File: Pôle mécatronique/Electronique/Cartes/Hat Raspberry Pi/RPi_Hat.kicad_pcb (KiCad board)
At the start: 2 copper layers, 65 x 59 mm, 29 parts, among them J1 Conn_02x03_Odd_Even, J2 RPi_GPIO, J3 Conn_01x02, U1 XBee, U2 MCP25625-x-SS, Y1 8MHz

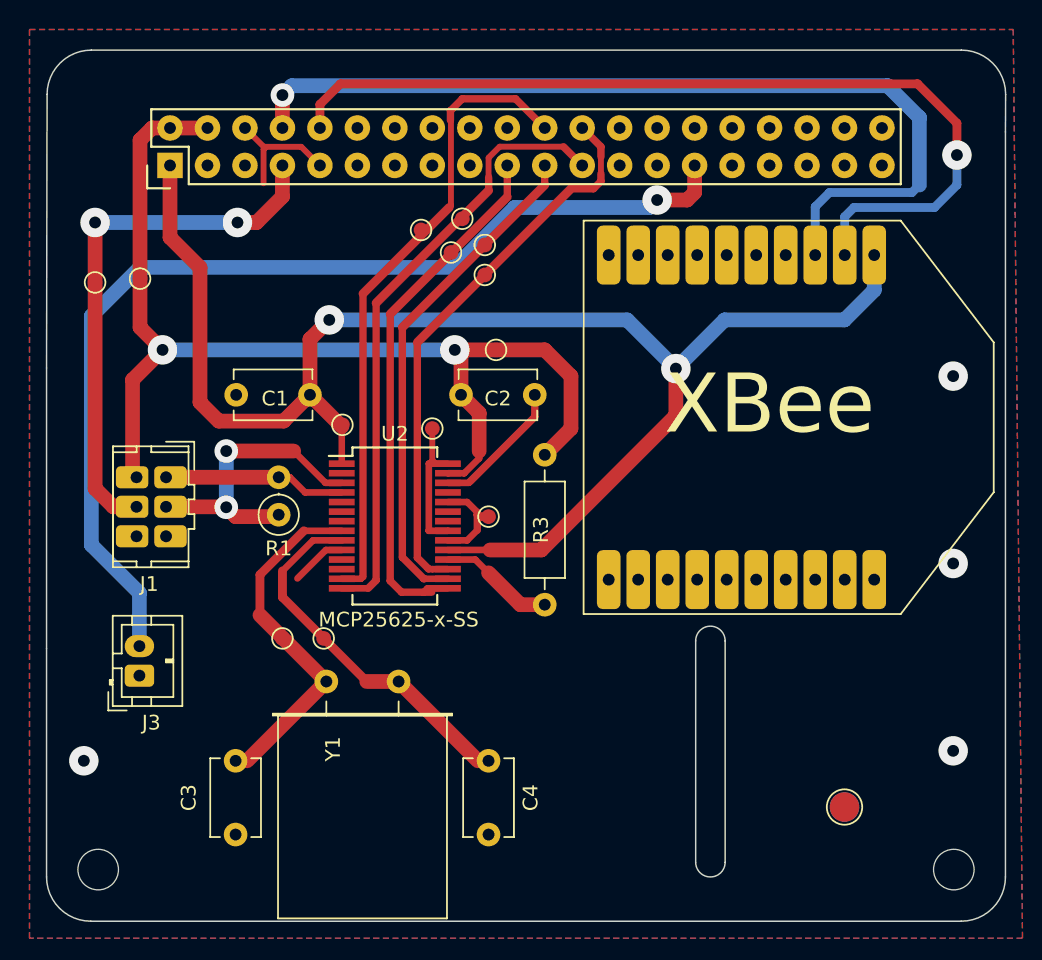
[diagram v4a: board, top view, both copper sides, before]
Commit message: Udpate HAT
Sérigraphie
Points de tests
Arret d'urgence
I2C
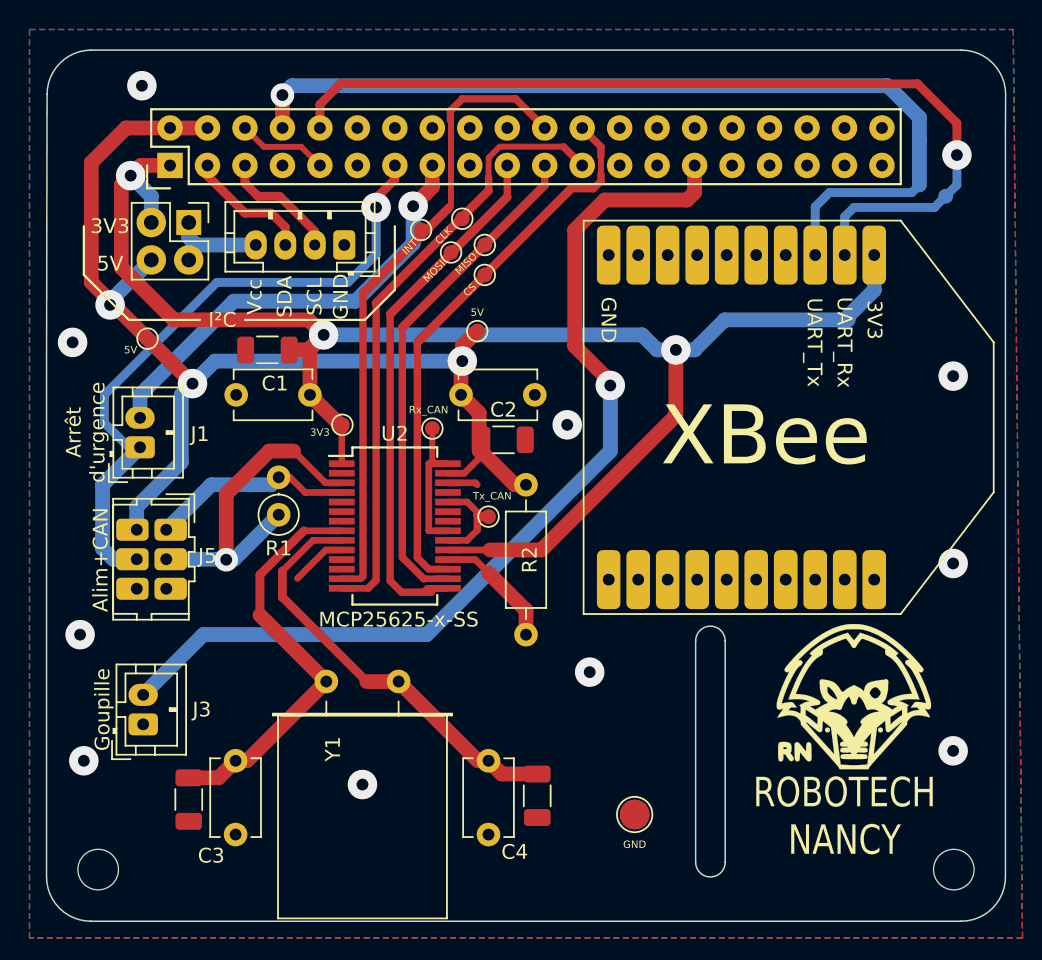
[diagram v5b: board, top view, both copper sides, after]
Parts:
- removed  : TestPoint_Pad_D1.0mm, TestPoint:TestPoint_Pad_D1.0mm (x2)
- removed the ? at (114.3, 86.4)
- removed R3: 5k, Resistor_THT:R_Axial_DIN0207_L6.3mm_D2.5mm_P10.16mm_Horizontal
- removed the REF** at (66.5, 50.5)
- removed the REF** at (114.3, 86.4)
- removed the REF** at (86.4, 60.7)
- removed the REF** at (87.6, 48.8)
- removed the REF** at (89.9, 48.3)
- removed the REF** at (90.7, 55.4)
- removed the REF** at (90.2, 66.7)
- removed the REF** at (88.4, 46.5)
- removed the REF** at (80.3, 60.5)
- removed the REF** at (89.9, 50.3)
- removed the REF** at (63.5, 50.8)
- added G***: LOGO, Logos:logoRobotechNancy10x10, F.Cu at (114.9, 78.7)
- added G***: LOGO, Logos:logoRobotechNancy10x10, B.Cu at (114.9, 78.7)
- added J1: Arrêt d'urgence, Connector_JST:JST_PH_B2B-PH-K_1x02_P2.00mm_Vertical, F.Cu at (66.5, 62.0)
- added J2: RPi_GPIO, Connector_JST:JST_PH_B4B-PH-K_1x04_P2.00mm_Vertical, F.Cu at (80.4, 48.3)
- added J4: Tension I2C, Connector_PinHeader_2.54mm:PinHeader_2x02_P2.54mm_Vertical, F.Cu at (69.8, 46.7)
- added R2: 5k, Resistor_THT:R_Axial_DIN0207_L6.3mm_D2.5mm_P10.16mm_Horizontal, F.Cu at (92.7, 64.5)
- added REF**: C_1206_3216Metric, Capacitor_SMD:C_1206_3216Metric, F.Cu at (93.5, 85.6)
- added REF**: C_1206_3216Metric, Capacitor_SMD:C_1206_3216Metric, F.Cu at (75.2, 55.4)
- added REF**: C_1206_3216Metric, Capacitor_SMD:C_1206_3216Metric, F.Cu at (69.8, 85.9)
- added REF**: C_1206_3216Metric, Capacitor_SMD:C_1206_3216Metric, F.Cu at (91.2, 61.5)
- added TP1: TestPoint, TestPoint:TestPoint_Pad_D1.0mm, B.Cu at (64.8, 63.8)
- added TP10: TestPoint, TestPoint:TestPoint_Pad_D1.0mm, F.Cu at (89.9, 50.3)
- added TP11: TestPoint, TestPoint:TestPoint_Pad_D1.0mm, B.Cu at (114.6, 53.3)
- added TP12: TestPoint, TestPoint:TestPoint_Pad_D1.0mm, F.Cu at (89.4, 54.1)
- added TP13: TestPoint, TestPoint:TestPoint_Pad_D1.0mm, F.Cu at (90.2, 66.7)
- added TP14: TestPoint, TestPoint:TestPoint_Pad_D1.0mm, F.Cu at (86.4, 60.7)
- added TP15: TestPoint, TestPoint:TestPoint_Pad_D2.0mm, F.Cu at (100.1, 86.9)
- added TP16: TestPoint, TestPoint:TestPoint_Pad_D2.0mm, B.Cu at (100.1, 86.9)
- added TP2: TestPoint, TestPoint:TestPoint_Pad_D1.0mm, B.Cu at (67.1, 57.9)
- added TP3: TestPoint, TestPoint:TestPoint_Pad_D1.0mm, B.Cu at (121.2, 45.0)
- added TP4: TestPoint, TestPoint:TestPoint_Pad_D1.0mm, B.Cu at (119.4, 41.1)
- added TP5: TestPoint, TestPoint:TestPoint_Pad_D1.0mm, F.Cu at (80.3, 60.5)
- added TP6: TestPoint, TestPoint:TestPoint_Pad_D1.0mm, F.Cu at (67.1, 54.6)
- added TP7: TestPoint, TestPoint:TestPoint_Pad_D1.0mm, F.Cu at (88.4, 46.5)
- added TP8: TestPoint, TestPoint:TestPoint_Pad_D1.0mm, F.Cu at (87.6, 48.8)
- added TP9: TestPoint, TestPoint:TestPoint_Pad_D1.0mm, F.Cu at (89.9, 48.3)
- J3: value Conn_01x02 -> Goupille
- J5: renamed from J1; value Conn_02x03_Odd_Even -> I2C
- J6: renamed from J2; value RPi_GPIO -> Vcc I2C
- moved J5 3.56 mm to (68.3, 67.6)
- moved J3 3.31 mm to (66.8, 80.8)
- renumbered REF** to Test_INT
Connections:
- J6 pad 13: unconnected-(J2-Pad13) -> cmd_relais
- J6 pad 15: unconnected-(J2-Pad15) -> /RPi_GPIO/cmd_relais_RPI
- J6 pad 3: unconnected-(J2-Pad3) -> SDA
- J6 pad 5: unconnected-(J2-Pad5) -> SCL
- J6 pad 7: cmd_relais -> unconnected-(J6-Pad7)
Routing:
- net /RPi_GPIO/cmd_relais_RPI: track 0.00 -> 30.1 mm, vias 0 -> 1
- net GND: track 24.5 -> 13.7 mm, vias 4 -> 10
- net SDA: track 0.00 -> 8.61 mm
- net SCL: track 0.00 -> 8.21 mm
- net cmd_relais: track 36.9 -> 44.4 mm, vias 2 -> 1
- net Net-(J2-Pad4): track 0.00 -> 7.35 mm
- net +3.3VA: track 102.1 -> 107.0 mm, vias 2 -> 3
- net /RPi_GPIO/Starter: track 69.9 -> 65.5 mm
- net +5V: track 74.4 -> 78.1 mm, vias 2 -> 3
- net Net-(C4-Pad1): track 25.2 -> 28.9 mm
- net Net-(C3-Pad1): track 24.3 -> 27.9 mm
- net can_L: track 20.5 -> 23.2 mm, vias 2 -> 1
- net can_H: track 12.3 -> 13.8 mm
- net Net-(R2-Pad2): track 7.83 -> 8.37 mm
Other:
- board text added: "3V3"
- board text added: "5V"
- board text added: "Alim+CAN"
- board text added: "Arrêt d'urgence"
- board text added: "CLK"
- board text added: "CS"
- board text added: "GND"
- board text added: "Goupille"
- board text added: "INT"
- board text added: "I²C"
- board text added: "MISO"
- board text added: "MOSI"
- board text added: "ROBOTECH NANCY"
- board text added: "Rx_CAN"
- board text added: "Rx_UART"
- board text added: "SCL"
- board text added: "SDA"
- board text added: "Tx_CAN"
- board text added: "Tx_UART"
- board text added: "UART_Rx"
- board text added: "UART_Tx"
- board text added: "Vcc"
- board text added: "cmd_relais"
- board text added: "cmd_relais_RPI"

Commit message: Correction pcb BR
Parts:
- moved Y1 1.02 mm to (79.2, 76.8)
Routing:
- net +3.3VA: track 107.0 -> 103.5 mm
- net Net-(C3-Pad1): track 27.9 -> 26.3 mm
- net MOSI: track 36.3 -> 35.2 mm
- net Net-(C4-Pad1): track 28.9 -> 28.0 mm
